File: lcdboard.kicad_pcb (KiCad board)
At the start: 2 copper layers, 64 x 120.5 mm, 72 parts, among them J1 Conn_01x06, J2 Conn_02x25_Counter_Clockwise, J3 Conn_02x12_Counter_Clockwise, J4 USB_B_Micro, J5 Conn_01x06, J6 Conn_01x02, SW1 SW_Push, SW3 SW_SPST, U1 MK82FN256VLL15, U2 Serial-Flash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

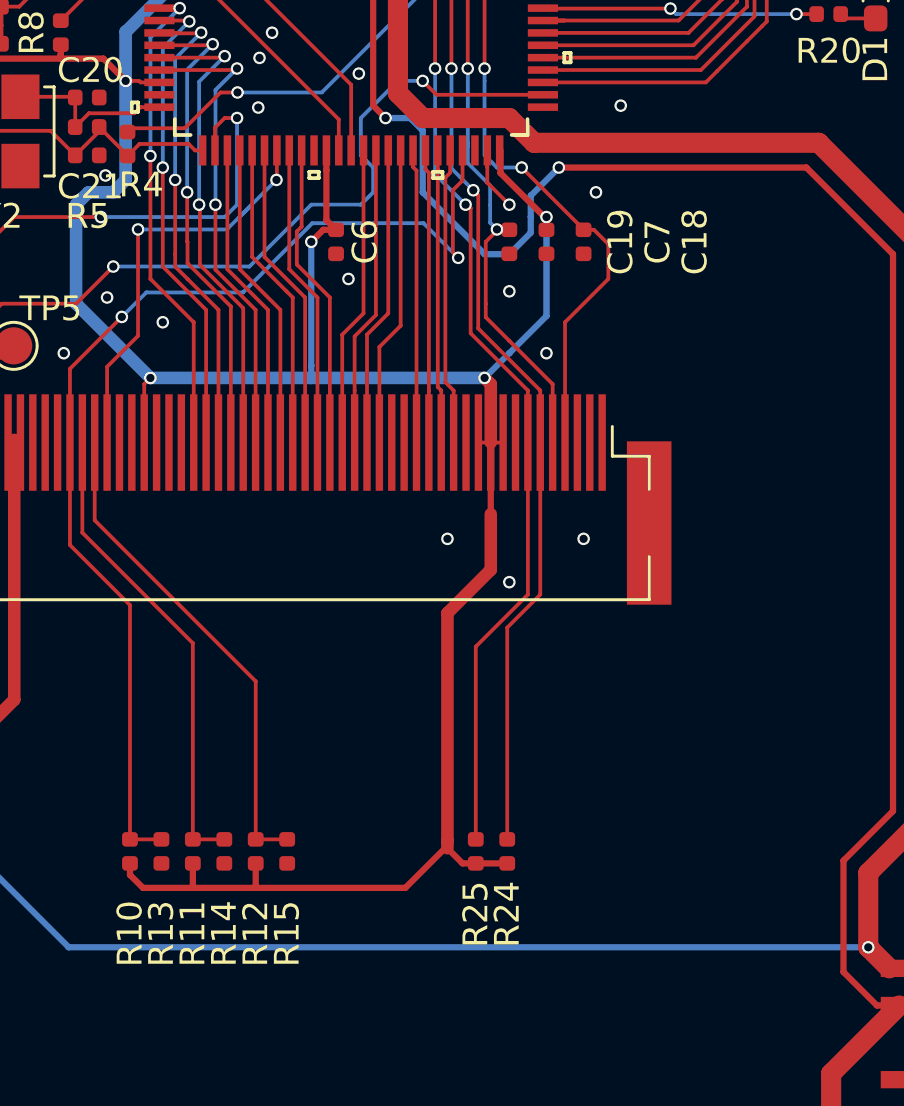
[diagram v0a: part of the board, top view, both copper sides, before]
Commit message: Add r-packs to LCD signals to reduce EMI
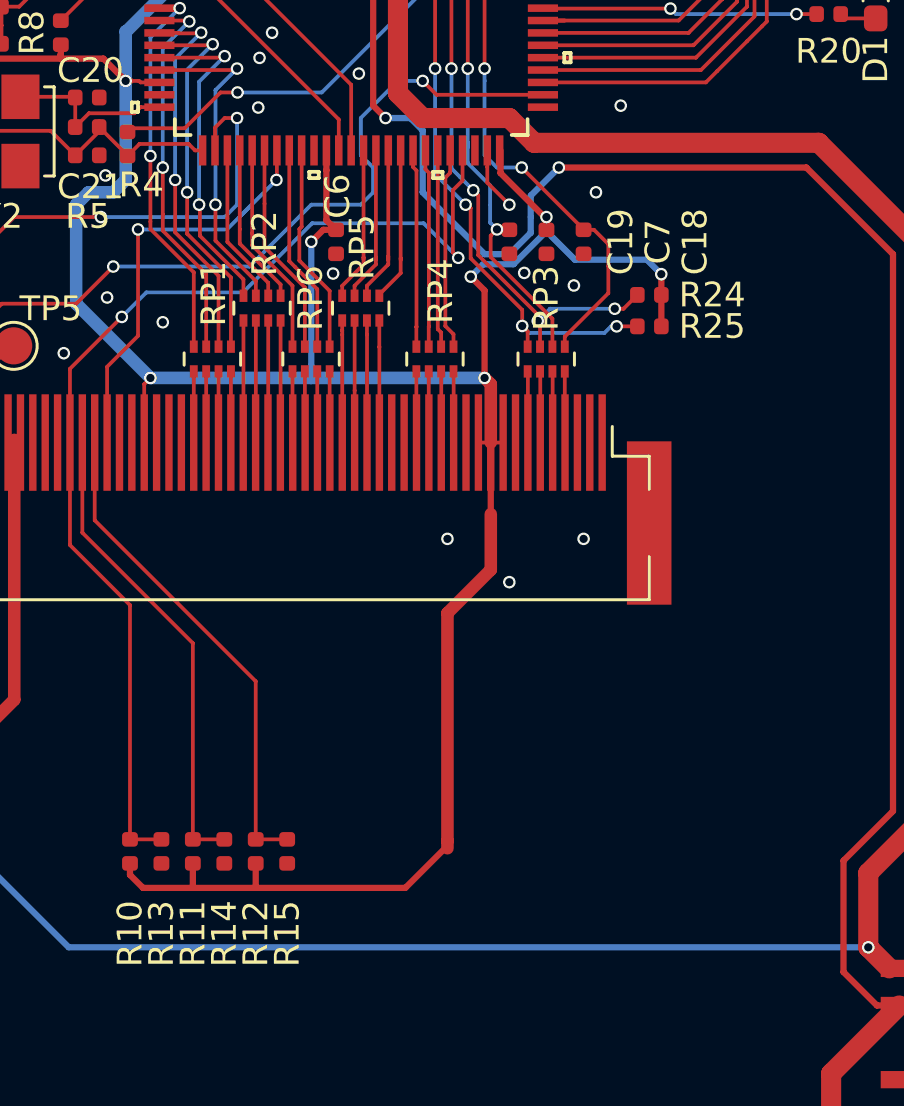
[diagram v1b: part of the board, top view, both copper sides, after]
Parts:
- added RP1: 200, Resistor_SMD:R_Array_Concave_4x0402, F.Cu at (-3.00, 10.2)
- added RP2: 200, Resistor_SMD:R_Array_Concave_4x0402, F.Cu at (-0.99, 8.18)
- added RP3: 200, Resistor_SMD:R_Array_Concave_4x0402, F.Cu at (10.5, 10.2)
- added RP4: 200, Resistor_SMD:R_Array_Concave_4x0402, F.Cu at (5.99, 10.2)
- added RP5: 200, Resistor_SMD:R_Array_Concave_4x0402, F.Cu at (3.00, 8.18)
- added RP6: 200, Resistor_SMD:R_Array_Concave_4x0402, F.Cu at (0.99, 10.2)
- moved R24 23.2 mm to (14.7, 7.65), turned to 180 degrees
- moved R25 22.3 mm to (14.7, 8.92), turned to 180 degrees
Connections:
- J2 pad 17: /DISP_DB15 -> Net-(J2-Pad17)
- J2 pad 18: /DISP_DB14 -> Net-(J2-Pad18)
- J2 pad 19: /DISP_DB13 -> Net-(J2-Pad19)
- J2 pad 20: /DISP_DB12 -> Net-(J2-Pad20)
- J2 pad 21: /DISP_DB11 -> Net-(J2-Pad21)
- J2 pad 22: /DISP_DB10 -> Net-(J2-Pad22)
- J2 pad 23: /DISP_DB9 -> Net-(J2-Pad23)
- J2 pad 24: /DISP_DB8 -> Net-(J2-Pad24)
- J2 pad 25: /DISP_DB7 -> Net-(J2-Pad25)
- J2 pad 26: /DISP_DB6 -> Net-(J2-Pad26)
- J2 pad 27: /DISP_DB5 -> Net-(J2-Pad27)
- J2 pad 28: /DISP_DB4 -> Net-(J2-Pad28)
- J2 pad 29: /DISP_DB3 -> Net-(J2-Pad29)
- J2 pad 30: /DISP_DB2 -> Net-(J2-Pad30)
- J2 pad 31: /DISP_DB1 -> Net-(J2-Pad31)
- J2 pad 32: /DISP_DB0 -> Net-(J2-Pad32)
- J2 pad 35: /DISP_RDX -> Net-(J2-Pad35)
- J2 pad 36: /DISP_WRX -> Net-(J2-Pad36)
- J2 pad 37: /DISP_DCX -> Net-(J2-Pad37)
- J2 pad 38: /DISP_CSX -> Net-(J2-Pad38)
- J2 pad 44: /CTP_SCL -> Net-(J2-Pad44)
- J2 pad 45: /CTP_SDA -> Net-(J2-Pad45)
- J2 pad 46: /CTP_INT -> Net-(J2-Pad46)
- J2 pad 47: /CTP_RST_b -> Net-(J2-Pad47)
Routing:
- net /CTP_SDA: track 47.3 -> 31.3 mm, vias 2 -> 4
- net /CTP_SCL: track 47.4 -> 31.5 mm, vias 2 -> 4
- net +3V3: track 228.7 -> 234.7 mm, vias 14 -> 16
- net /DISP_DB11: track 19.4 -> 13.5 mm
- net /DISP_DB8: track 12.5 -> 6.55 mm
- net /DISP_DB9: track 12.5 -> 6.55 mm
- net /DISP_DB10: track 19.3 -> 13.4 mm
- net /DISP_DB0: track 12.2 -> 6.31 mm
- net /DISP_DB3: track 12.2 -> 6.31 mm
- net /DISP_DB2: track 12.2 -> 6.33 mm
- net /DISP_DB1: track 12.2 -> 6.38 mm
- net Net-(J2-Pad24): track 0.00 -> 4.94 mm
- net Net-(J2-Pad23): track 0.00 -> 4.94 mm
- net Net-(J2-Pad22): track 0.00 -> 4.94 mm
- net Net-(J2-Pad21): track 0.00 -> 4.94 mm
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
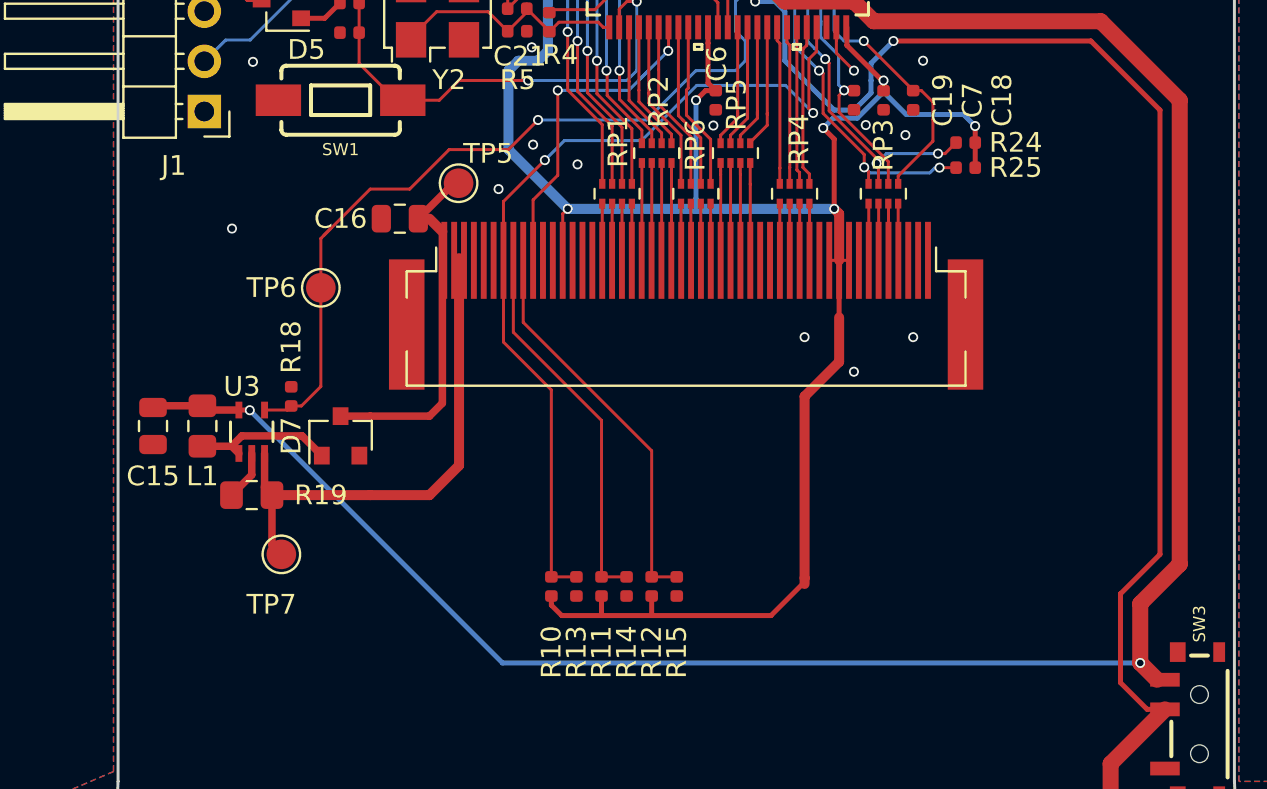
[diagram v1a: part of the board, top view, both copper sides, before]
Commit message: Reposition backlight driver
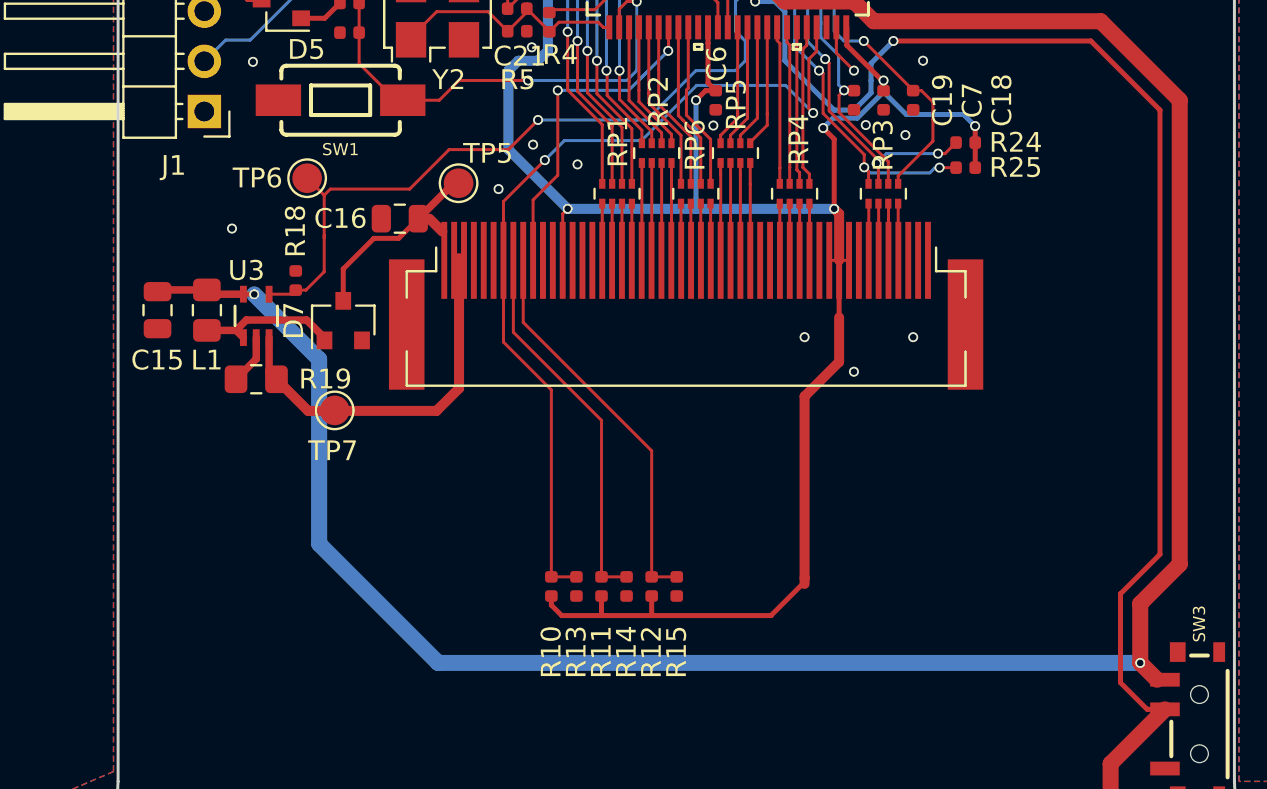
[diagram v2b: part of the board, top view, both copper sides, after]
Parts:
- moved TP7 7.78 mm to (-17.3, 21.2)
- moved C15 5.87 mm to (-26.3, 16.1)
- moved L1 5.87 mm to (-23.8, 16.1)
- moved R18 5.87 mm to (-19.3, 14.6)
- moved R19 5.87 mm to (-21.3, 19.6)
- moved U3 5.87 mm to (-21.9, 17.5)
- moved D7 5.84 mm to (-16.9, 16.7)
- moved TP6 5.59 mm to (-18.7, 9.45)
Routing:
- net /VDD_REGIN: track 165.5 -> 173.2 mm
- net /BKLT_A: track 17.8 -> 10.1 mm
- net /BKLT_K: track 26.1 -> 19.2 mm
- net /BKLT_PWM: track 48.2 -> 44.1 mm
